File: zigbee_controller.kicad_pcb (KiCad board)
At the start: 2 copper layers, 55.5 x 62.9 mm, 74 parts, among them J1 KF635, J10 TerminalBlock_KF301-5.0, J11 TerminalBlock_KF301-5.0, J12 TerminalBlock_KF301-5.0, J13 TerminalBlock_KF301-5.0, J3 Conn_01x06, J4 Conn_01x07, J5 Conn_01x05, P1 USB_C_Receptacle_GCT_USB4105, Q2 IRLB3813, Q3 IRLB3813, Q4 IRLB3813, Q5 IRLB3813, SW2 EN, SW4 Boot, U1 TPS54560, U2 ESP32-C6-MINI-1, U4 TC4427, U5 TC4427, U6 RT9080, U9 CH224K

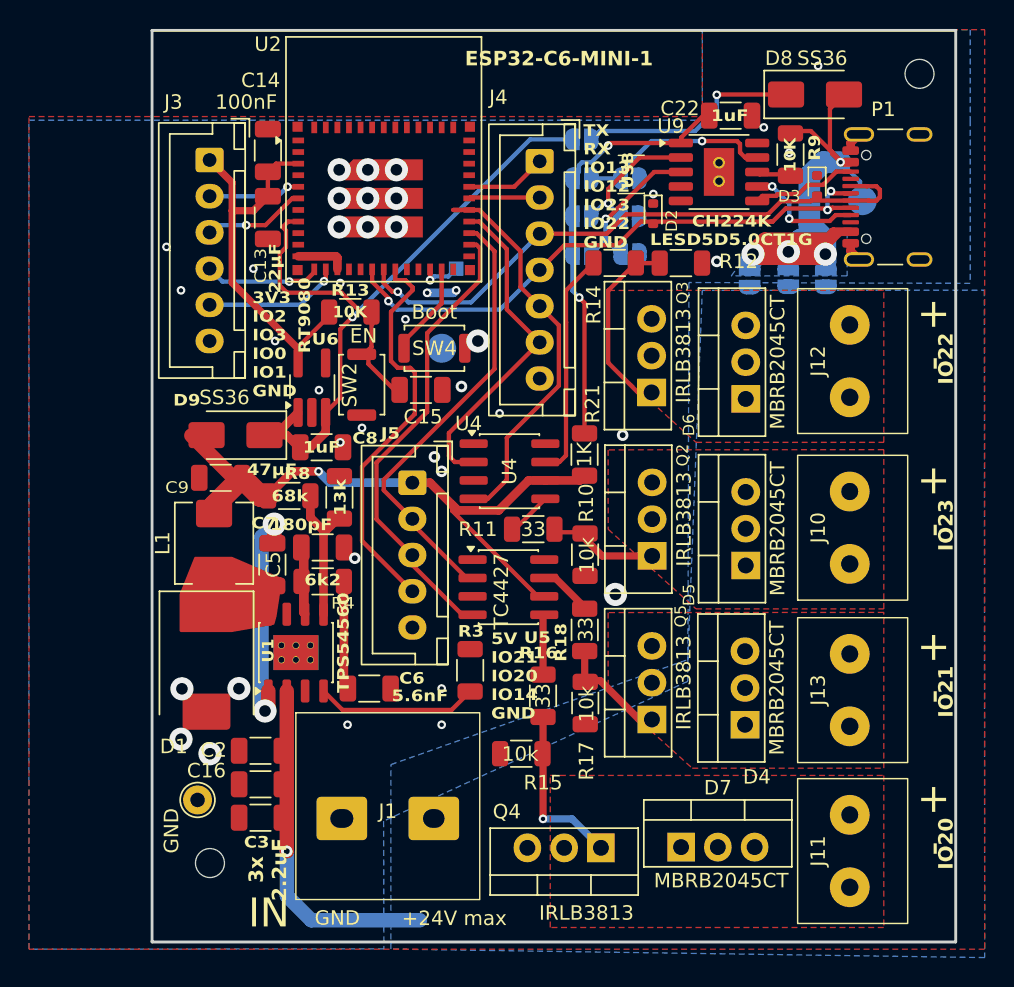
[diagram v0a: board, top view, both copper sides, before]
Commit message: Fixed silkscreen, added components on silkscreen
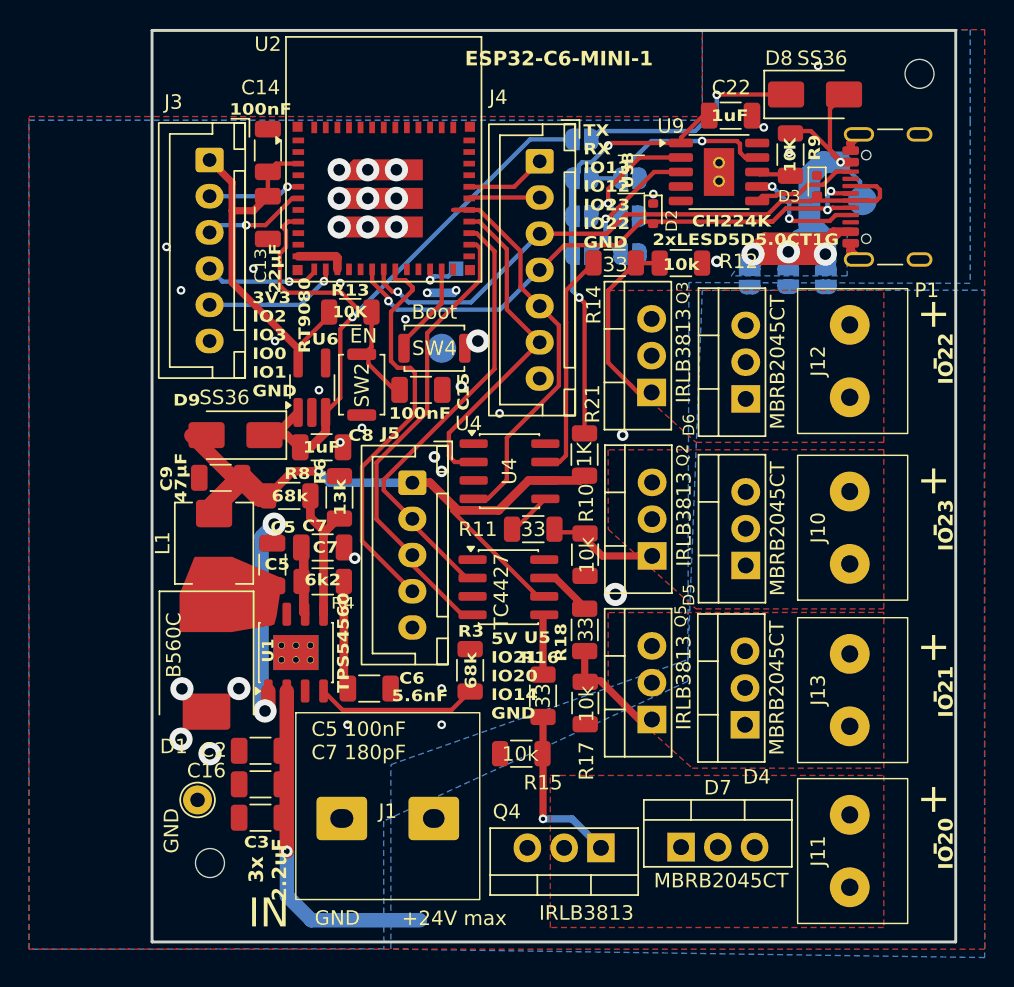
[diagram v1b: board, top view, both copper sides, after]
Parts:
- D3: value LESD5D5.0CT1G -> 2xLESD5D5.0CT1G
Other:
- board text added: "- 2oz copper - U1: TPS54560 - U4/U5: TC4427 - U6: XT9080 - U9: CH224K - D1: B650C - J1: KF635 - Q2-Q5: IRLB3813 - SW1/SW2: 3x4x2 switch - L1: 1040 10μH inductor 0530 - J10-J13: KF301-5.0 - D4-D7: Optional fly-back diode MBRB2045CT (Schottky)"
- board text added: "C5"
- board text added: "C5 100nF C7 180pF"
- board text added: "C7"
- board text added: "|V |CFG1|CFG2|CFG3| |---|----|----|----| |5V | 1 | 0 | 0 | |9V | 0 | 0 | 0 | |12V| 0 | 0 | 1 | |15V| 0 | 1 | 1 | |20V| 0 | 1 | 0"
- board text removed: "- 2oz copper - U1: TPS54560 - U4/U5: TC4427 - U6: XT9080 - U9: CH224K - D1: B650C - Q2-Q5: IRLB3813 - L1: 1040 10μH inductor 0530 - J10-J13: MKDS 5mm terminals - D4-D7: Optional fly-back diode MBRB2045CT (Schottky)"
- board text removed: "| V | CFG1 | CFG2 | CFG3 | |-----|------|------|------| | 5V | 1 | 0 | 0 | | 9V | 0 | 0 | 0 | | 12V | 0 | 0 | 1 | | 15V | 0 | 1 | 1 | | 20V | 0 | 1 | 0 |"

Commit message: Added github repositiory link to backside
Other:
- board text added: "git@github.com:DavoudTaghawiNejad/zigbee_led_controller.git"

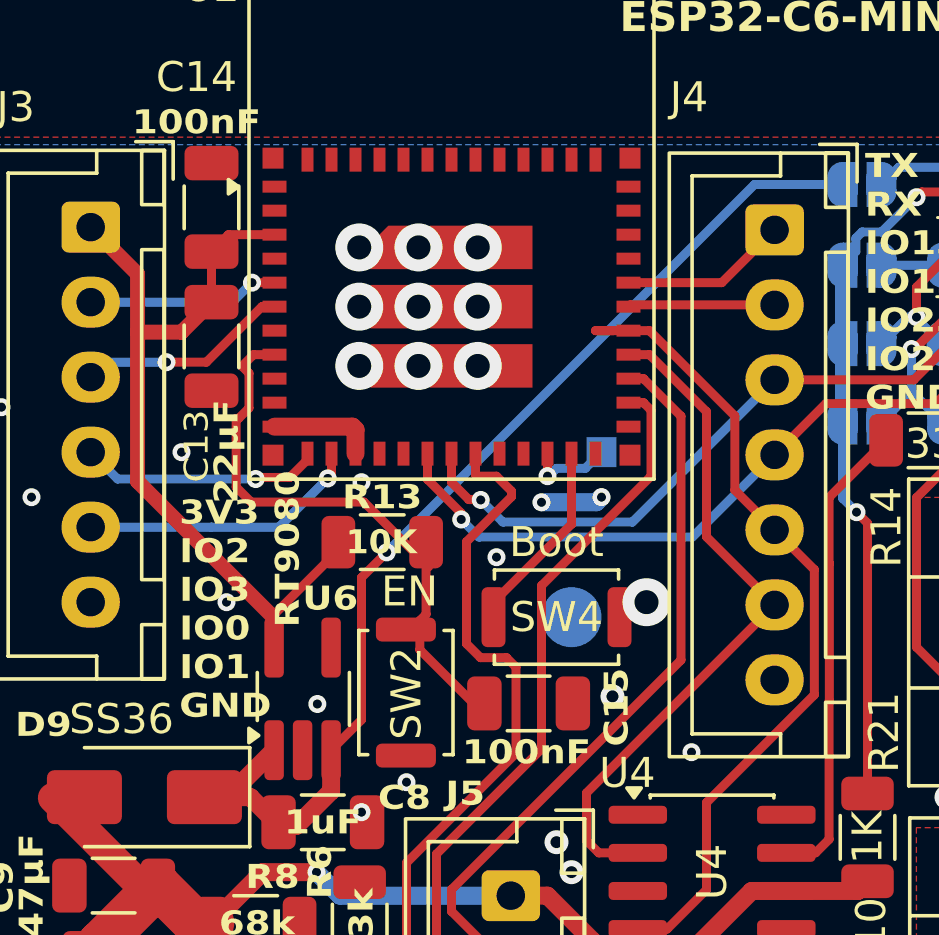
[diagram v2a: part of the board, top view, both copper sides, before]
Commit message: Improved cooling of XT9080, more GND plane
even bigger ground plane
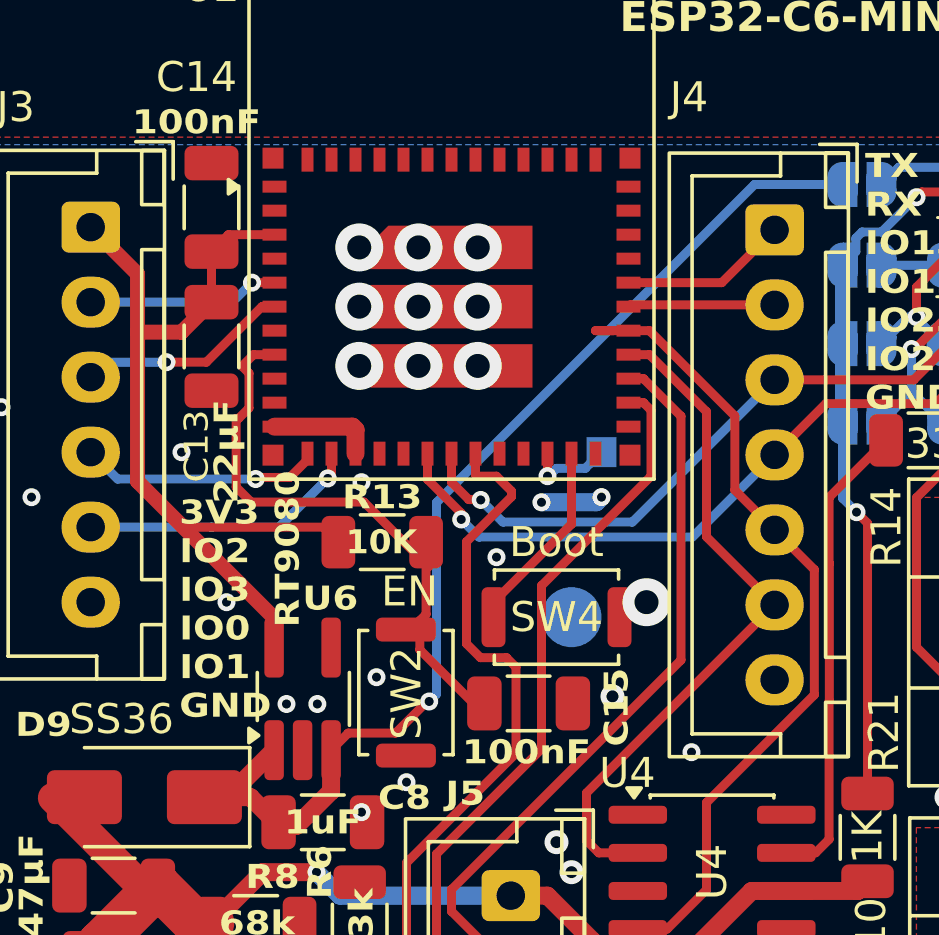
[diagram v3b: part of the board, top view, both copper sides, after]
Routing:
- net 3V3: track 25.4 -> 32.1 mm
- net USB_5V: track 36.3 -> 37.3 mm
- net GND: vias 40 -> 42
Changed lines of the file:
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@@
+	)
+	(via
+		(at 163 94.844571)
+		(size 0.6)
+		(drill 0.3)
+		(layers "F.Cu" "B.Cu")
+		(free yes)
+		(net "GND")
 	)
 	(via
@@
 	)
 	(via
+		(at 166 93.95)
+		(size 0.6)
+		(drill 0.3)
+		(layers "F.Cu" "B.Cu")
+		(free yes)
+		(net "GND")
+	)
+	(via
 		(at 170 89.95)
 		(size 0.6)
@@
 	)
 	(segment
+		(start 166.636379 95.813621)
+		(end 165.057461 95.813621)
+		(width 0.3)
+		(layer "F.Cu")
+		(net "USB_5V")
+	)
+	(segment
 		(start 161.798959 97.95)
 		(end 162.756206 98.907247)
@@
 	)
 	(segment
+		(start 167.710052 94.739948)
+		(end 166.636379 95.813621)
+		(width 0.3)
+		(layer "F.Cu")
+		(net "USB_5V")
+	)
+	(segment
 		(start 161.021082 97.95)
 		(end 162.586717 96.384365)
@@
 	)
 	(segment
-		(start 165.5 95.371082)
-		(end 164.486717 96.384365)
+		(start 167.755553 94.760523)
+		(end 167.734978 94.739948)
 		(width 0.3)
 		(layer "F.Cu")
@@
 	)
 	(segment
+		(start 167.734978 94.739948)
+		(end 167.710052 94.739948)
+		(width 0.3)
+		(layer "F.Cu")
+		(net "USB_5V")
+	)
+	(segment
+		(start 165.057461 95.813621)
+		(end 164.486717 96.384365)
+		(width 0.3)
+		(layer "F.Cu")
+		(net "USB_5V")
+	)
+	(segment
 		(start 164.486717 97.751736)
 		(end 164.486717 96.384365)
@@
 	)
 	(segment
-		(start 165.5 90.629782)
-		(end 165.5 95.371082)
-		(width 0.3)
-		(layer "F.Cu")
-		(net "USB_5V")
-	)
-	(segment
 		(start 162.756206 98.907247)
 		(end 163.331206 98.907247)
@@
 		(net "USB_5V")
 	)
-	(segment
-		(start 166.339891 89.789891)
-		(end 165.5 90.629782)
-		(width 0.3)
-		(layer "F.Cu")
-		(net "USB_5V")
-	)
-	(via
-		(at 166.339891 89.789891)
-		(size 0.6)
-		(drill 0.3)
-		(layers "F.Cu" "B.Cu")
+	(via
+		(at 167.755553 94.760523)
+		(size 0.6)
+		(drill 0.3)
+		(layers "F.Cu" "B.Cu")
+		(net "USB_5V")
+	)
+	(segment
+		(start 167.755553 94.760523)
+		(end 168 94.516076)
+		(width 0.3)
+		(layer "B.Cu")
+		(net "USB_5V")
+	)
+	(segment
+		(start 168 94.516076)
+		(end 168 88.129781)
+		(width 0.3)
+		(layer "B.Cu")
+		(net "USB_5V")
+	)
+	(segment
+		(start 168 88.129781)
+		(end 178.602016 77.527765)
+		(width 0.3)
+		(layer "B.Cu")
 		(net "USB_5V")
 	)
@@
 		(start 178.602016 77.527765)
 		(end 181.53401 77.527765)
-		(width 0.3)
-		(layer "B.Cu")
-		(net "USB_5V")
-	)
-	(segment
-		(start 166.339891 89.789891)
-		(end 178.602016 77.527765)
 		(width 0.3)
 		(layer "B.Cu")
@@
 	)
 	(segment
+		(start 164.728551 89.45)
+		(end 164.228551 88.95)
+		(width 0.3)
+		(layer "F.Cu")
+		(net "3V3")
+	)
+	(segment
 		(start 162.462721 91.853582)
 		(end 162.462721 91.85206)
@@
 	)
 	(segment
-		(start 164.728551 89.721449)
+		(start 164.228551 88.95)
+		(end 159.6 88.95)
+		(width 0.3)
+		(layer "F.Cu")
+		(net "3V3")
+	)
+	(segment
+		(start 159.6 88.95)
 		(end 162.55 91.9)
 		(width 0.3)
@@
 		(layer "F.Cu")
 		(net "3V3")
+	)
+	(segment
+		(start 164.728551 89.721449)
+		(end 164.728551 89.45)
+		(width 0.3)
+		(layer "F.Cu")
+		(net "3V3")

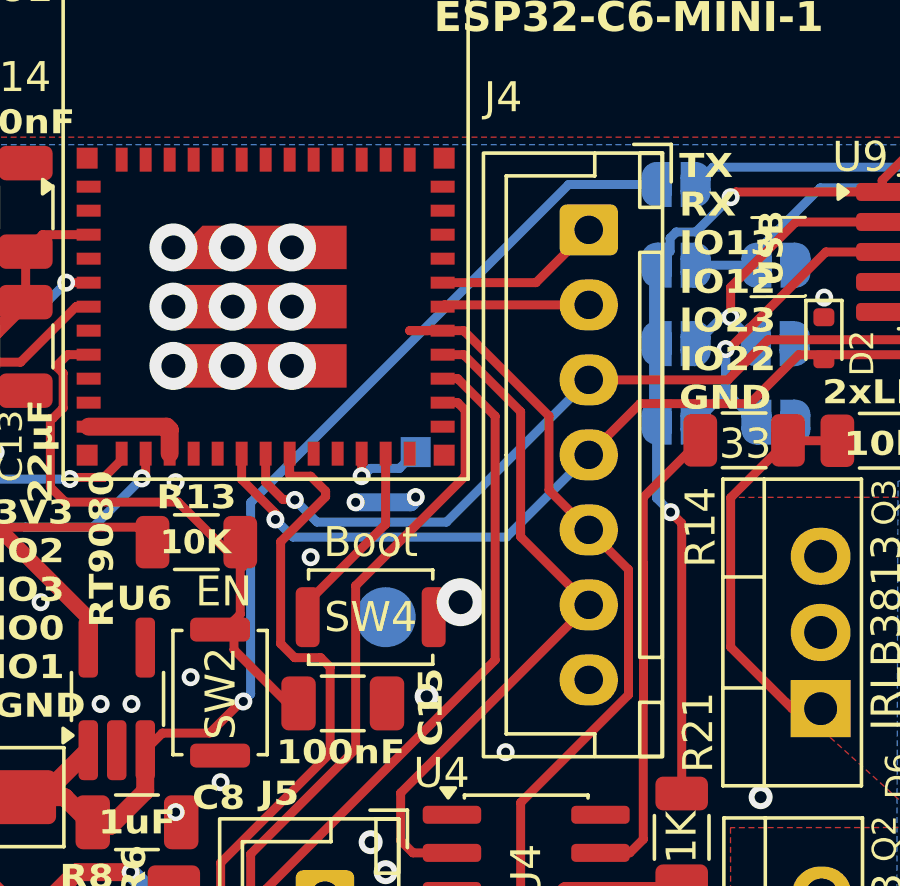
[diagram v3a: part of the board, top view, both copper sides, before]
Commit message: Increase cooling backside groundplane for ESP32
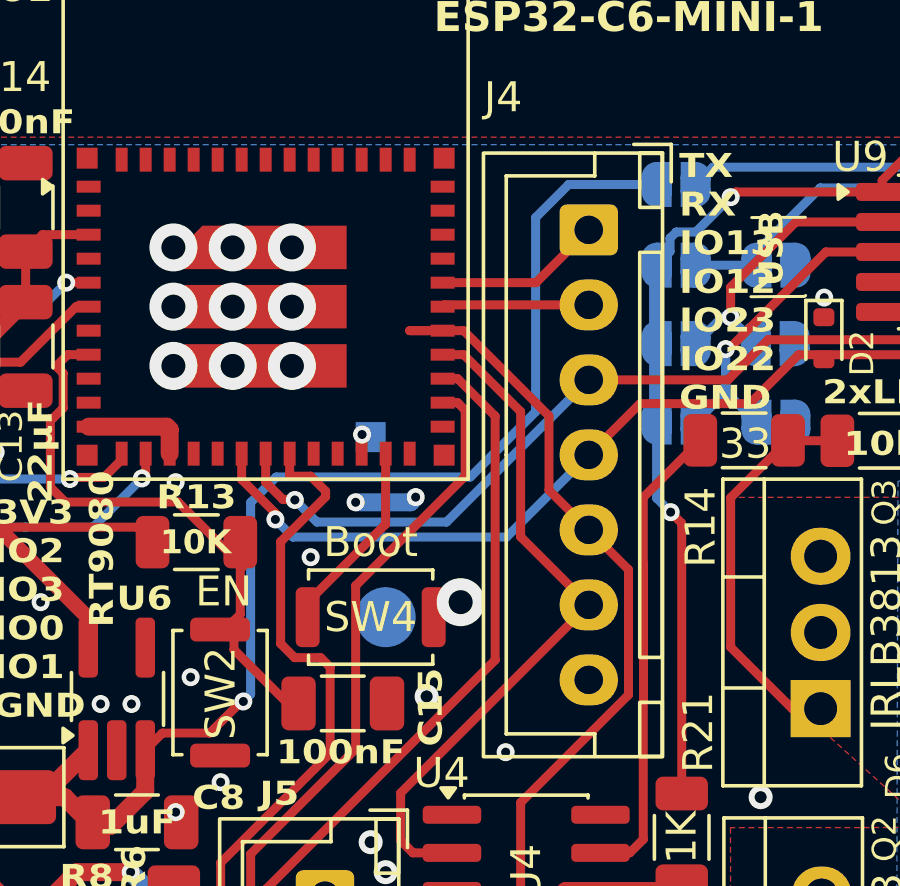
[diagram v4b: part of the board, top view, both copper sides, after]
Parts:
- moved TP1 1.58 mm to (172.0, 86.0)
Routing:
- net USB_5V: track 37.3 -> 41.1 mm
- net Net-(U2-IO8): track 2.88 -> 1.32 mm
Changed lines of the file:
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@@
 	(footprint "TestPoint:TestPoint_Pad_1.0x1.0mm"
 		(layer "B.Cu")
-		(at 173.5 86.45 180)
+		(at 172 85.95 180)
 		(descr "SMD rectangular pad as test Point, square 1.0mm side length")
 		(tags "test point SMD pad rectangle square")
@@
 	)
 	(segment
-		(start 167.755553 94.760523)
-		(end 168 94.516076)
+		(start 178.602016 77.527765)
+		(end 177.5 78.629781)
 		(width 0.3)
 		(layer "B.Cu")
@@
 	)
 	(segment
-		(start 168 94.516076)
+		(start 168.850747 87.279034)
 		(end 168 88.129781)
 		(width 0.3)
@@
 	)
 	(segment
-		(start 168 88.129781)
+		(start 177.5 78.629781)
+		(end 177.5 85.103131)
+		(width 0.3)
+		(layer "B.Cu")
+		(net "USB_5V")
+	)
+	(segment
+		(start 175.324097 87.279034)
+		(end 168.850747 87.279034)
+		(width 0.3)
+		(layer "B.Cu")
+		(net "USB_5V")
+	)
+	(segment
+		(start 177.5 85.103131)
+		(end 175.324097 87.279034)
+		(width 0.3)
+		(layer "B.Cu")
+		(net "USB_5V")
+	)
+	(segment
+		(start 168 94.516076)
+		(end 167.755553 94.760523)
+		(width 0.3)
+		(layer "B.Cu")
+		(net "USB_5V")
+	)
+	(segment
+		(start 181.53401 77.527765)
 		(end 178.602016 77.527765)
 		(width 0.3)
@@
 	)
 	(segment
-		(start 178.602016 77.527765)
-		(end 181.53401 77.527765)
+		(start 168 88.129781)
+		(end 168 94.516076)
 		(width 0.3)
 		(layer "B.Cu")
@@
 	)
 	(segment
-		(start 171.7 86.5)
-		(end 171.7 87.25)
+		(start 171.712867 86.487133)
+		(end 171.7 86.5)
 		(width 0.3)
 		(layer "F.Cu")
 		(net "Net-(U2-IO8)")
 	)
-	(via
-		(at 171.7 87.25)
-		(size 0.6)
-		(drill 0.3)
-		(layers "F.Cu" "B.Cu")
-		(net "Net-(U2-IO8)")
-	)
 	(segment
-		(start 172 86.989908)
-		(end 172.960092 86.989908)
+		(start 171.7 86.5)
+		(end 171.7 86.15)
 		(width 0.3)
-		(layer "B.Cu")
+		(layer "F.Cu")
 		(net "Net-(U2-IO8)")
 	)
 	(segment
-		(start 171.825372 87.164536)
-		(end 172 86.989908)
+		(start 171.712867 85.861489)
+		(end 171.712867 86.487133)
 		(width 0.3)
-		(layer "B.Cu")
+		(layer "F.Cu")
 		(net "Net-(U2-IO8)")
 	)
-	(segment
-		(start 172.960092 86.989908)
-		(end 173.5 86.45)
-		(width 0.3)
-		(layer "B.Cu")
+	(via
+		(at 171.712867 85.861489)
+		(size 0.6)
+		(drill 0.3)
+		(layers "F.Cu" "B.Cu")
 		(net "Net-(U2-IO8)")
 	)
 	(segment
-		(start 171.785464 87.164536)
-		(end 171.825372 87.164536)
+		(start 171.712867 85.861489)
+		(end 171.801378 85.95)
 		(width 0.3)
 		(layer "B.Cu")
@@
 	)
 	(segment
-		(start 171.7 87.25)
-		(end 171.785464 87.164536)
+		(start 171.801378 85.95)
+		(end 172 85.95)
 		(width 0.3)
 		(layer "B.Cu")

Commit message: some optimizations
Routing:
- net GND: track 8.33 -> 6.26 mm, vias 42 -> 40
- net /IO23: track 27.4 -> 25.9 mm
- net Net-(U2-EN): track 19.3 -> 20.5 mm
- net /IO12-usb: track 42.1 -> 43.3 mm
- net USB_5V: track 41.1 -> 40.2 mm
- net /IO13-usb: track 41.1 -> 41.9 mm
- net Net-(D8-K): track 15.3 -> 14.8 mm
